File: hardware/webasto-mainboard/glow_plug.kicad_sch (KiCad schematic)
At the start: 25 parts, among them Q11 SSM3J374R, Q12 2N7002, Q13 SUD50P04-08, Q14 SUD50P04-08, Q15 SUD50P04-08, Q16 SUD50P04-08, Q17 SUD50P04-08, Q18 2N7002, Q19 2N7002, U6 LM7805_TO220, U7 INA219BxDCN

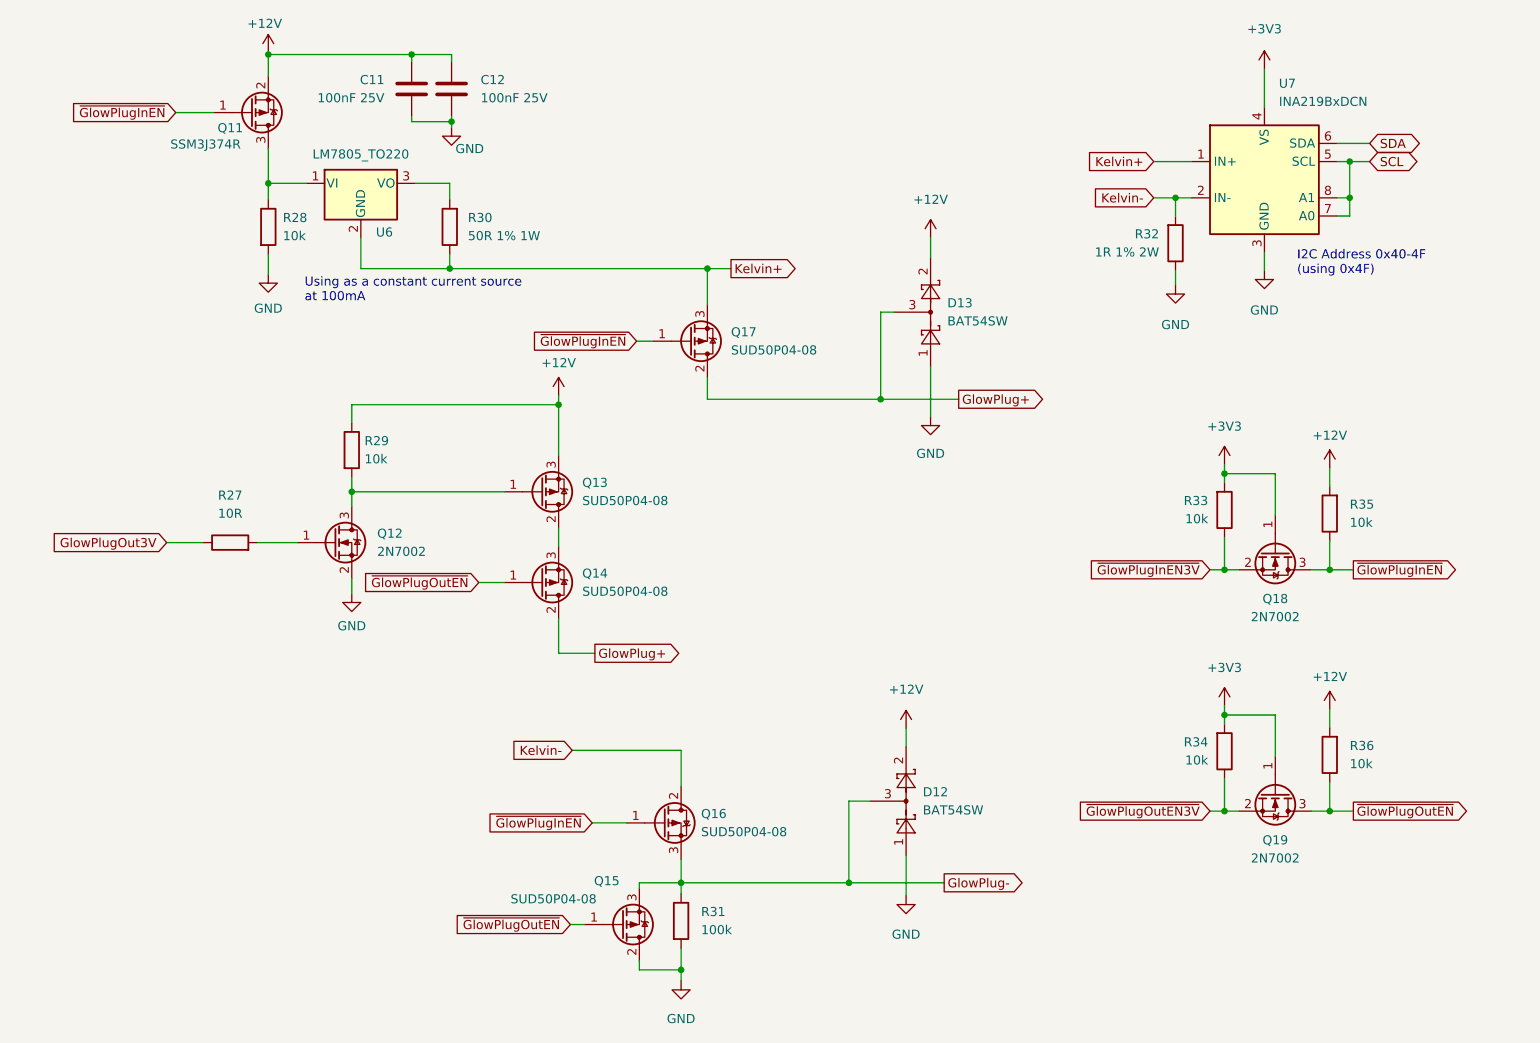
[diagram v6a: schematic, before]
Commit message: Moved emerg. shutdown offboard
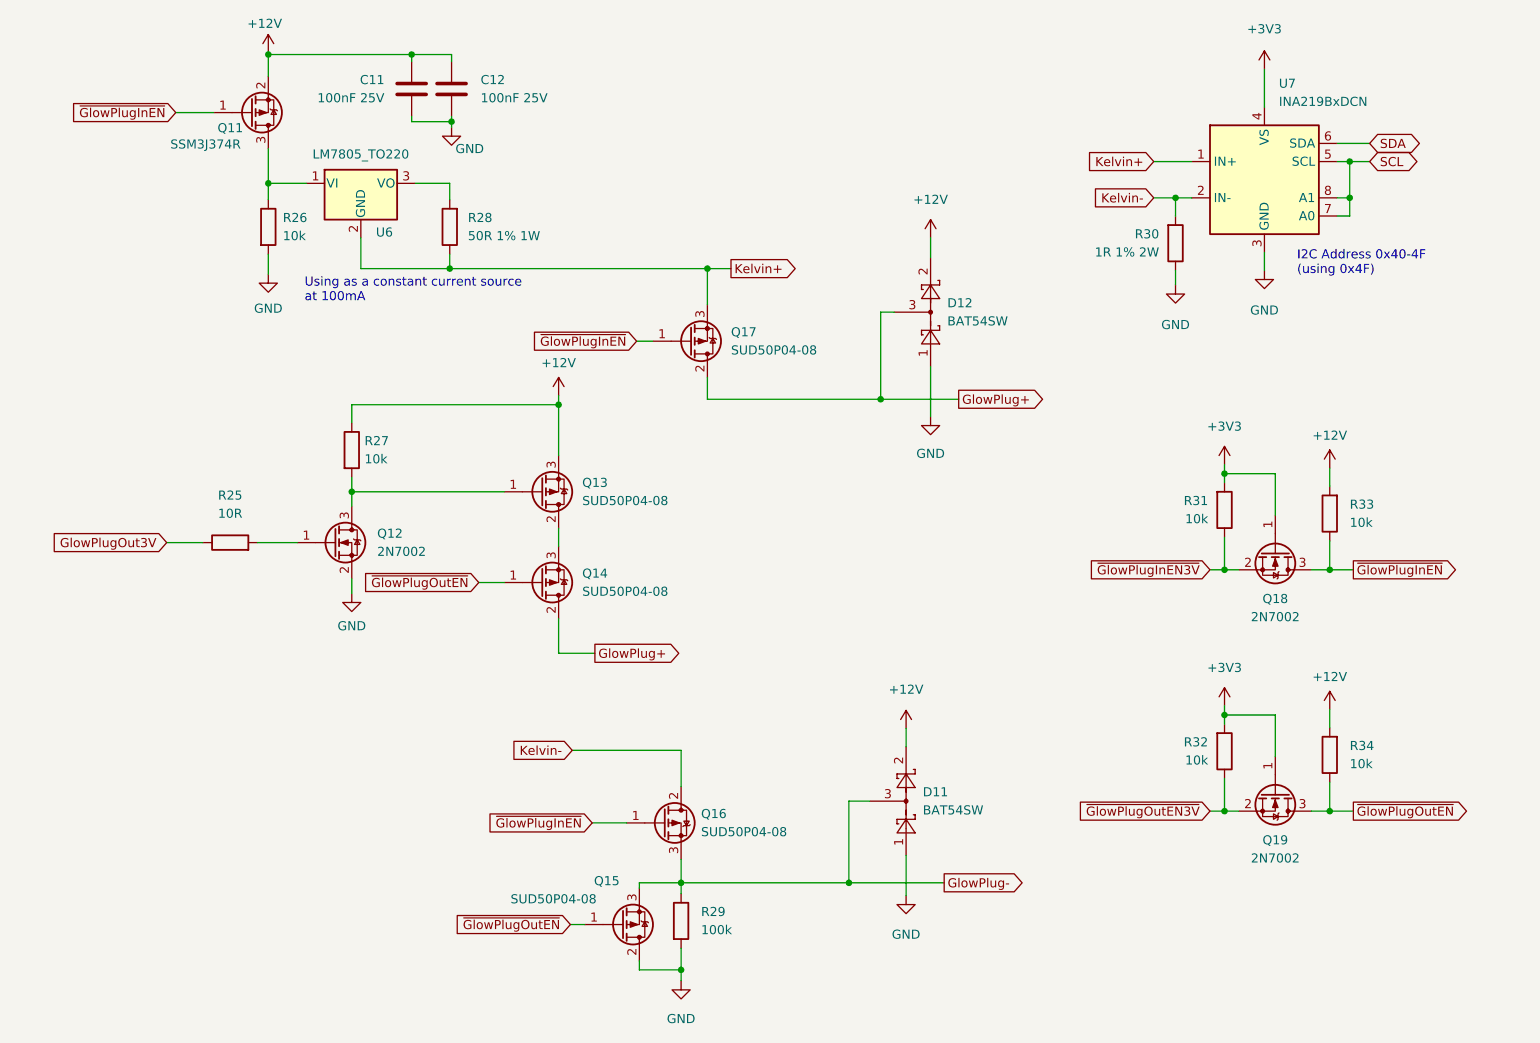
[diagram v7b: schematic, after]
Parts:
- renumbered D12 to D11, D13 to D12, R27 to R25, R28 to R26, R29 to R27, R30 to R28, R31 to R29, R32 to R30, R33 to R31, R34 to R32, R35 to R33, R36 to R34
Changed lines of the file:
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@@
   (title_block
     (title "Webasto Replacement Mainboard (Thermo Top C)")
-    (date "2023-01-31")
-    (rev "v1.0")
+    (date "2023-02-10")
+    (rev "2.0")
     (company "Gavin Hurlbut")
   )
@@
   (symbol (lib_name "+3V3_1") (lib_id "power:+3V3") (at 202.565 29.972 0) (unit 1)
     (in_bom yes) (on_board yes) (fields_autoplaced)
-    (property "Reference" "#PWR077" (id 0) (at 202.565 33.782 0)
+    (property "Reference" "#PWR076" (id 0) (at 202.565 33.782 0)
       (effects (font (size 1.27 1.27)) hide)
     )
@@
   (symbol (lib_name "GND_8") (lib_id "power:GND") (at 202.565 58.166 0) (unit 1)
     (in_bom yes) (on_board yes) (fields_autoplaced)
-    (property "Reference" "#PWR078" (id 0) (at 202.565 64.516 0)
+    (property "Reference" "#PWR077" (id 0) (at 202.565 64.516 0)
       (effects (font (size 1.27 1.27)) hide)
     )
@@
   (symbol (lib_id "Device:R") (at 120.904 149.225 0) (unit 1)
     (in_bom yes) (on_board yes) (fields_autoplaced)
-    (property "Reference" "R31" (id 0) (at 123.698 147.9549 0)
+    (property "Reference" "R29" (id 0) (at 123.698 147.9549 0)
       (effects (font (size 1.27 1.27)) (justify left))
     )
@@
   (symbol (lib_id "power:+12V") (at 155.829 53.594 0) (unit 1)
     (in_bom yes) (on_board yes) (fields_autoplaced)
-    (property "Reference" "#PWR072" (id 0) (at 155.829 57.404 0)
+    (property "Reference" "#PWR071" (id 0) (at 155.829 57.404 0)
       (effects (font (size 1.27 1.27)) hide)
     )
@@
   (symbol (lib_id "Device:R") (at 74.803 83.312 0) (unit 1)
     (in_bom yes) (on_board yes) (fields_autoplaced)
-    (property "Reference" "R29" (id 0) (at 76.581 82.0419 0)
+    (property "Reference" "R27" (id 0) (at 76.581 82.0419 0)
       (effects (font (size 1.27 1.27)) (justify left))
     )
@@
   (symbol (lib_id "Device:R") (at 88.519 52.07 180) (unit 1)
     (in_bom yes) (on_board yes)
-    (property "Reference" "R30" (id 0) (at 91.059 50.7999 0)
+    (property "Reference" "R28" (id 0) (at 91.059 50.7999 0)
       (effects (font (size 1.27 1.27)) (justify right))
     )
@@
   (symbol (lib_name "+3V3_2") (lib_id "power:+3V3") (at 196.977 85.344 0) (unit 1)
     (in_bom yes) (on_board yes) (fields_autoplaced)
-    (property "Reference" "#PWR075" (id 0) (at 196.977 89.154 0)
+    (property "Reference" "#PWR074" (id 0) (at 196.977 89.154 0)
       (effects (font (size 1.27 1.27)) hide)
     )
@@
   (symbol (lib_name "GND_2") (lib_id "power:GND") (at 74.803 103.378 0) (unit 1)
     (in_bom yes) (on_board yes) (fields_autoplaced)
-    (property "Reference" "#PWR066" (id 0) (at 74.803 109.728 0)
+    (property "Reference" "#PWR065" (id 0) (at 74.803 109.728 0)
       (effects (font (size 1.27 1.27)) hide)
     )
@@
   (symbol (lib_id "Device:R") (at 63.119 52.07 0) (unit 1)
     (in_bom yes) (on_board yes)
-    (property "Reference" "R28" (id 0) (at 65.151 50.7999 0)
+    (property "Reference" "R26" (id 0) (at 65.151 50.7999 0)
       (effects (font (size 1.27 1.27)) (justify left))
     )
@@
   (symbol (lib_name "+3V3_2") (lib_id "power:+3V3") (at 196.977 119.126 0) (unit 1)
     (in_bom yes) (on_board yes) (fields_autoplaced)
-    (property "Reference" "#PWR076" (id 0) (at 196.977 122.936 0)
+    (property "Reference" "#PWR075" (id 0) (at 196.977 122.936 0)
       (effects (font (size 1.27 1.27)) hide)
     )
@@
   (symbol (lib_id "Device:R") (at 57.785 96.266 90) (unit 1)
     (in_bom yes) (on_board yes) (fields_autoplaced)
-    (property "Reference" "R27" (id 0) (at 57.785 89.662 90))
+    (property "Reference" "R25" (id 0) (at 57.785 89.662 90))
     (property "Value" "10R" (id 1) (at 57.785 92.202 90))
     (property "Footprint" "Resistor_SMD:R_0805_2012Metric_Pad1.20x1.40mm_HandSolder" (id 2) (at 57.785 98.044 90)
@@
   (symbol (lib_id "Diode:BAT54SW") (at 152.4 132.461 270) (mirror x) (unit 1)
     (in_bom yes) (on_board yes) (fields_autoplaced)
-    (property "Reference" "D12" (id 0) (at 154.7368 131.1909 90)
+    (property "Reference" "D11" (id 0) (at 154.7368 131.1909 90)
       (effects (font (size 1.27 1.27)) (justify left))
     )
@@
   (symbol (lib_id "Device:R") (at 196.977 125.476 0) (mirror x) (unit 1)
     (in_bom yes) (on_board yes) (fields_autoplaced)
-    (property "Reference" "R34" (id 0) (at 194.691 124.2059 0)
+    (property "Reference" "R32" (id 0) (at 194.691 124.2059 0)
       (effects (font (size 1.27 1.27)) (justify right))
     )
@@
   (symbol (lib_name "GND_9") (lib_id "power:GND") (at 120.904 157.607 0) (unit 1)
     (in_bom yes) (on_board yes) (fields_autoplaced)
-    (property "Reference" "#PWR069" (id 0) (at 120.904 163.957 0)
+    (property "Reference" "#PWR068" (id 0) (at 120.904 163.957 0)
       (effects (font (size 1.27 1.27)) hide)
     )
@@
   (symbol (lib_name "+12V_3") (lib_id "power:+12V") (at 211.709 85.852 0) (unit 1)
     (in_bom yes) (on_board yes) (fields_autoplaced)
-    (property "Reference" "#PWR079" (id 0) (at 211.709 89.662 0)
+    (property "Reference" "#PWR078" (id 0) (at 211.709 89.662 0)
       (effects (font (size 1.27 1.27)) hide)
     )
@@
   (symbol (lib_name "GND_5") (lib_id "power:GND") (at 88.773 38.1 0) (unit 1)
     (in_bom yes) (on_board yes)
-    (property "Reference" "#PWR067" (id 0) (at 88.773 44.45 0)
+    (property "Reference" "#PWR066" (id 0) (at 88.773 44.45 0)
       (effects (font (size 1.27 1.27)) hide)
     )
@@
   (symbol (lib_id "Device:R") (at 211.709 92.202 180) (unit 1)
     (in_bom yes) (on_board yes) (fields_autoplaced)
-    (property "Reference" "R35" (id 0) (at 214.503 90.9319 0)
+    (property "Reference" "R33" (id 0) (at 214.503 90.9319 0)
       (effects (font (size 1.27 1.27)) (justify right))
     )
@@
   (symbol (lib_id "power:GND") (at 155.829 78.613 0) (unit 1)
     (in_bom yes) (on_board yes) (fields_autoplaced)
-    (property "Reference" "#PWR073" (id 0) (at 155.829 84.963 0)
+    (property "Reference" "#PWR072" (id 0) (at 155.829 84.963 0)
       (effects (font (size 1.27 1.27)) hide)
     )
@@
   (symbol (lib_name "GND_8") (lib_id "power:GND") (at 190.119 60.198 0) (unit 1)
     (in_bom yes) (on_board yes) (fields_autoplaced)
-    (property "Reference" "#PWR074" (id 0) (at 190.119 66.548 0)
+    (property "Reference" "#PWR073" (id 0) (at 190.119 66.548 0)
       (effects (font (size 1.27 1.27)) hide)
     )
@@
   (symbol (lib_name "+12V_2") (lib_id "power:+12V") (at 63.119 27.686 0) (unit 1)
     (in_bom yes) (on_board yes)
-    (property "Reference" "#PWR064" (id 0) (at 63.119 31.496 0)
+    (property "Reference" "#PWR063" (id 0) (at 63.119 31.496 0)
       (effects (font (size 1.27 1.27)) hide)
     )
@@
   (symbol (lib_name "+12V_3") (lib_id "power:+12V") (at 211.709 119.634 0) (unit 1)
     (in_bom yes) (on_board yes) (fields_autoplaced)
-    (property "Reference" "#PWR080" (id 0) (at 211.709 123.444 0)
+    (property "Reference" "#PWR079" (id 0) (at 211.709 123.444 0)
       (effects (font (size 1.27 1.27)) hide)
     )
@@
   (symbol (lib_id "Diode:BAT54SW") (at 155.829 64.008 270) (mirror x) (unit 1)
     (in_bom yes) (on_board yes) (fields_autoplaced)
-    (property "Reference" "D13" (id 0) (at 158.1658 62.7379 90)
+    (property "Reference" "D12" (id 0) (at 158.1658 62.7379 90)
       (effects (font (size 1.27 1.27)) (justify left))
     )
@@
   (symbol (lib_id "power:GND") (at 152.4 145.669 0) (unit 1)
     (in_bom yes) (on_board yes) (fields_autoplaced)
-    (property "Reference" "#PWR071" (id 0) (at 152.4 152.019 0)
+    (property "Reference" "#PWR070" (id 0) (at 152.4 152.019 0)
       (effects (font (size 1.27 1.27)) hide)
     )
@@
   (symbol (lib_id "power:+12V") (at 152.4 122.301 0) (unit 1)
     (in_bom yes) (on_board yes) (fields_autoplaced)
-    (property "Reference" "#PWR070" (id 0) (at 152.4 126.111 0)
+    (property "Reference" "#PWR069" (id 0) (at 152.4 126.111 0)
       (effects (font (size 1.27 1.27)) hide)
     )
@@
   (symbol (lib_name "GND_3") (lib_id "power:GND") (at 63.119 58.674 0) (unit 1)
     (in_bom yes) (on_board yes) (fields_autoplaced)
-    (property "Reference" "#PWR065" (id 0) (at 63.119 65.024 0)
+    (property "Reference" "#PWR064" (id 0) (at 63.119 65.024 0)
       (effects (font (size 1.27 1.27)) hide)
     )
@@
   (symbol (lib_id "Device:R") (at 211.709 125.984 180) (unit 1)
     (in_bom yes) (on_board yes) (fields_autoplaced)
-    (property "Reference" "R36" (id 0) (at 214.503 124.7139 0)
+    (property "Reference" "R34" (id 0) (at 214.503 124.7139 0)
       (effects (font (size 1.27 1.27)) (justify right))
     )
@@
   (symbol (lib_id "Device:R") (at 190.119 54.356 0) (mirror x) (unit 1)
     (in_bom yes) (on_board yes) (fields_autoplaced)
-    (property "Reference" "R32" (id 0) (at 187.833 53.0859 0)
+    (property "Reference" "R30" (id 0) (at 187.833 53.0859 0)
       (effects (font (size 1.27 1.27)) (justify right))
     )
@@
   (symbol (lib_name "+12V_1") (lib_id "power:+12V") (at 103.759 75.692 0) (unit 1)
     (in_bom yes) (on_board yes) (fields_autoplaced)
-    (property "Reference" "#PWR068" (id 0) (at 103.759 79.502 0)
+    (property "Reference" "#PWR067" (id 0) (at 103.759 79.502 0)
       (effects (font (size 1.27 1.27)) hide)
     )
@@
   (symbol (lib_id "Device:R") (at 196.977 91.694 0) (mirror x) (unit 1)
     (in_bom yes) (on_board yes) (fields_autoplaced)
-    (property "Reference" "R33" (id 0) (at 194.691 90.4239 0)
-      (effects (font (size 1.27 1.27)) (justify right))
-    )
+    (property "Reference" "R31" (id 0) (at 194.691 90.4239 0)
+      (effects (font (size 1.27 1.27)) (justify right))
+    )
